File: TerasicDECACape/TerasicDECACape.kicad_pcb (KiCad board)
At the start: 4 copper layers, 61.3 x 66.3 mm, 34 parts, among them CN1 NASB0-S6701-TS50, CN2 NASB0-S6701-TS50, J1 MiSTer SDRAM Module, J2 USB_A, J3 Conn_01x03_Male, J4 Conn_02x06_Odd_Even, M1 Sipeed Lichee, P8 BeagleBone_Black_Header, P9 BeagleBone_Black_Header, SW1 TS-1187A-B-A-B, SW2 TS-1187A-B-A-B

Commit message: tidy, make it ready for production
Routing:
- net +3V3: track 8.53 -> 15.4 mm, vias 0 -> 6
- net /PB8_UART0_TX: vias 1 -> 2
- net /PB9_UART0_RX: vias 1 -> 2
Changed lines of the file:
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@@
     (fp_line (start 2.12 1.09) (end 0.93 1.09) (layer "F.SilkS") (width 0.15))
     (fp_line (start -2.27 -0.94) (end -2.27 0.94) (layer "F.SilkS") (width 0.15))
-    (fp_arc (start 0.001269 0.002199) (mid -0.112199 -0.41873) (end 0 -0.84) (layer "F.SilkS") (width 0.08))
+    (fp_arc (start 0.001269 0.002199) (mid -0.112199 -0.418731) (end 0 -0.84) (layer "F.SilkS") (width 0.08))
     (fp_arc (start -0.001269 -0.002199) (mid 0.112199 0.41873) (end 0 0.84) (layer "F.SilkS") (width 0.08))
     (fp_circle (center -1.6 0.8) (end -1.57 0.8) (layer "F.Fab") (width 0.06) (fill none))
@@
   (segment (start 115.1915 58.546) (end 115.1915 63.7438) (width 0.25) (layer "F.Cu") (net 65))
   (segment (start 116.3701 57.3674) (end 115.1915 58.546) (width 0.25) (layer "F.Cu") (net 65))
+  (via (at 128.5621 70.1294) (size 0.75) (drill 0.6) (layers "F.Cu" "B.Cu") (free) (net 65))
+  (via (at 137.9601 114.5794) (size 0.75) (drill 0.6) (layers "F.Cu" "B.Cu") (free) (net 65))
+  (via (at 137.9601 78.1304) (size 0.75) (drill 0.6) (layers "F.Cu" "B.Cu") (free) (net 65))
+  (via (at 128.5621 72.4154) (size 0.75) (drill 0.6) (layers "F.Cu" "B.Cu") (free) (net 65))
+  (via (at 140.2461 78.1304) (size 0.75) (drill 0.6) (layers "F.Cu" "B.Cu") (free) (net 65))
+  (via (at 140.2461 114.5794) (size 0.75) (drill 0.6) (layers "F.Cu" "B.Cu") (free) (net 65))
+  (segment (start 137.9601 114.5794) (end 140.2461 114.5794) (width 0.6) (layer "B.Cu") (net 65))
+  (segment (start 137.9601 78.1304) (end 140.2461 78.1304) (width 0.6) (layer "B.Cu") (net 65))
+  (segment (start 128.5621 72.4154) (end 128.5621 70.1294) (width 0.6) (layer "B.Cu") (net 65))
   (segment (start 134.4001 117.3324) (end 137.0701 117.3324) (width 0.3) (layer "F.Cu") (net 66))
   (segment (start 124.5201 68.7324) (end 125.0701 68.1824) (width 1.5) (layer "F.Cu") (net 66))
@@
   (segment (start 136.11571 99.8324) (end 150.267905 113.984595) (width 0.3) (layer "F.Cu") (net 155))
   (via (at 150.267905 113.984595) (size 0.6) (drill 0.4) (layers "F.Cu" "B.Cu") (net 155))
-  (segment (start 165.9915 119.441) (end 167.1701 118.2624) (width 0.25) (layer "B.Cu") (net 155))
-  (segment (start 153.20931 116.926) (end 155.72431 119.441) (width 0.25) (layer "B.Cu") (net 155))
-  (segment (start 155.72431 119.441) (end 165.9915 119.441) (width 0.25) (layer "B.Cu") (net 155))
-  (segment (start 150.267905 113.984595) (end 153.20931 116.926) (width 0.3) (layer "B.Cu") (net 155))
+  (segment (start 150.267905 113.984595) (end 150.884611 113.367889) (width 0.25) (layer "B.Cu") (net 155))
+  (segment (start 157.2641 115.4684) (end 162.5981 115.4684) (width 0.25) (layer "B.Cu") (net 155))
+  (segment (start 164.227589 117.097889) (end 166.005589 117.097889) (width 0.25) (layer "B.Cu") (net 155))
+  (segment (start 166.005589 117.097889) (end 167.1701 118.2624) (width 0.25) (layer "B.Cu") (net 155))
+  (segment (start 162.5981 115.4684) (end 164.227589 117.097889) (width 0.25) (layer "B.Cu") (net 155))
+  (segment (start 155.163589 113.367889) (end 157.2641 115.4684) (width 0.25) (layer "B.Cu") (net 155))
+  (segment (start 150.884611 113.367889) (end 155.163589 113.367889) (width 0.25) (layer "B.Cu") (net 155))
   (segment (start 136.5201 99.3324) (end 151.1701 113.9824) (width 0.3) (layer "F.Cu") (net 156))
   (segment (start 134.3901 99.3324) (end 136.5201 99.3324) (width 0.3) (layer "F.Cu") (net 156))
   (via (at 151.1701 113.9824) (size 0.6) (drill 0.4) (layers "F.Cu" "B.Cu") (net 156))
-  (segment (start 152.9101 115.7224) (end 155.4501 118.2624) (width 0.25) (layer "B.Cu") (net 156))
-  (segment (start 155.4501 118.2624) (end 164.6301 118.2624) (width 0.25) (layer "B.Cu") (net 156))
-  (segment (start 151.1701 113.9824) (end 152.9101 115.7224) (width 0.3) (layer "B.Cu") (net 156))
+  (segment (start 154.8891 113.9824) (end 157.2641 116.3574) (width 0.25) (layer "B.Cu") (net 156))
+  (segment (start 157.2641 116.3574) (end 162.7251 116.3574) (width 0.25) (layer "B.Cu") (net 156))
+  (segment (start 162.7251 116.3574) (end 164.6301 118.2624) (width 0.25) (layer "B.Cu") (net 156))
+  (segment (start 151.1701 113.9824) (end 154.8891 113.9824) (width 0.25) (layer "B.Cu") (net 156))
   (segment (start 125.7451 91.9324) (end 123.5451 94.1324) (width 0.3) (layer "F.Cu") (net 157))
   (segment (start 123.5451 94.1324) (end 117.6401 94.1324) (width 0.3) (layer "F.Cu") (net 157))
@@
   (segment (start 130.4701 76.6824) (end 130.4701 76.6719) (width 0.3) (layer "F.Cu") (net 166))
   (segment (start 130.4701 76.6719) (end 130.9701 76.1719) (width 0.3) (layer "F.Cu") (net 166))
+  (segment (start 134.6581 72.2884) (end 134.7001 72.2464) (width 0.25) (layer "F.Cu") (net 166))
   (segment (start 126.8501 93.4324) (end 128.148064 93.4324) (width 0.3) (layer "F.Cu") (net 166))
   (segment (start 135.2201 63.7824) (end 135.2201 65.3124) (width 0.3) (layer "F.Cu") (net 166))
+  (segment (start 134.7001 72.2464) (end 134.7001 65.8324) (width 0.25) (layer "F.Cu") (net 166))
   (segment (start 130.4701 91.110364) (end 130.4701 76.6824) (width 0.3) (layer "F.Cu") (net 166))
   (segment (start 128.148064 93.4324) (end 130.4701 91.110364) (width 0.3) (layer "F.Cu") (net 166))
+  (via (at 134.6581 72.2884) (size 0.6) (drill 0.4) (layers "F.Cu" "B.Cu") (net 166))
   (via (at 130.9701 76.1719) (size 0.6) (drill 0.4) (layers "F.Cu" "B.Cu") (net 166))
+  (segment (start 134.6701 74.163844) (end 134.6701 72.3004) (width 0.25) (layer "B.Cu") (net 166))
   (segment (start 132.662044 76.1719) (end 134.6701 74.163844) (width 0.3) (layer "B.Cu") (net 166))
+  (segment (start 134.6701 72.3004) (end 134.6581 72.2884) (width 0.25) (layer "B.Cu") (net 166))
   (segment (start 130.9701 76.1719) (end 132.662044 76.1719) (width 0.3) (layer "B.Cu") (net 166))
-  (segment (start 134.7001 70.1024) (end 134.7001 65.8324) (width 0.3) (layer "B.Cu") (net 166))
-  (segment (start 134.6701 70.1324) (end 134.7001 70.1024) (width 0.3) (layer "B.Cu") (net 166))
-  (segment (start 134.6701 74.163844) (end 134.6701 70.1324) (width 0.3) (layer "B.Cu") (net 166))
   (segment (start 127.9551 92.9324) (end 129.6701 91.2174) (width 0.3) (layer "F.Cu") (net 167))
   (segment (start 126.8501 92.9324) (end 127.9551 92.9324) (width 0.3) (layer "F.Cu") (net 167))
+  (segment (start 133.3881 72.2884) (end 132.1601 71.0604) (width 0.25) (layer "F.Cu") (net 167))
   (segment (start 129.6701 91.2174) (end 129.6701 76.4324) (width 0.3) (layer "F.Cu") (net 167))
   (segment (start 129.6701 76.4324) (end 129.6701 76.1824) (width 0.3) (layer "F.Cu") (net 167))
+  (segment (start 132.1601 71.0604) (end 132.1601 65.8324) (width 0.25) (layer "F.Cu") (net 167))
   (segment (start 129.6701 76.1824) (end 130.3201 75.5324) (width 0.3) (layer "F.Cu") (net 167))
   (segment (start 131.6701 65.3424) (end 132.1601 65.8324) (width 0.3) (layer "F.Cu") (net 167))
   (segment (start 131.6701 63.8324) (end 131.6701 65.3424) (width 0.3) (layer "F.Cu") (net 167))
+  (via (at 133.3881 72.2884) (size 0.6) (drill 0.4) (layers "F.Cu" "B.Cu") (net 167))
   (via (at 130.3201 75.5324) (size 0.6) (drill 0.4) (layers "F.Cu" "B.Cu") (net 167))
   (segment (start 130.3201 75.5324) (end 132.60858 75.5324) (width 0.3) (layer "B.Cu") (net 167))
-  (segment (start 133.4601 74.68088) (end 133.4601 67.1324) (width 0.3) (layer "B.Cu") (net 167))
-  (segment (start 133.4601 67.1324) (end 132.1601 65.8324) (width 0.3) (layer "B.Cu") (net 167))
+  (segment (start 133.4601 74.68088) (end 133.4601 72.3604) (width 0.25) (layer "B.Cu") (net 167))
+  (segment (start 133.4601 72.3604) (end 133.3881 72.2884) (width 0.25) (layer "B.Cu") (net 167))
   (segment (start 132.60858 75.5324) (end 133.4601 74.68088) (width 0.3) (layer "B.Cu") (net 167))
   (segment (start 155.5651 116.0624) (end 155.5651 115.2174) (width 0.3) (layer "F.Cu") (net 168))

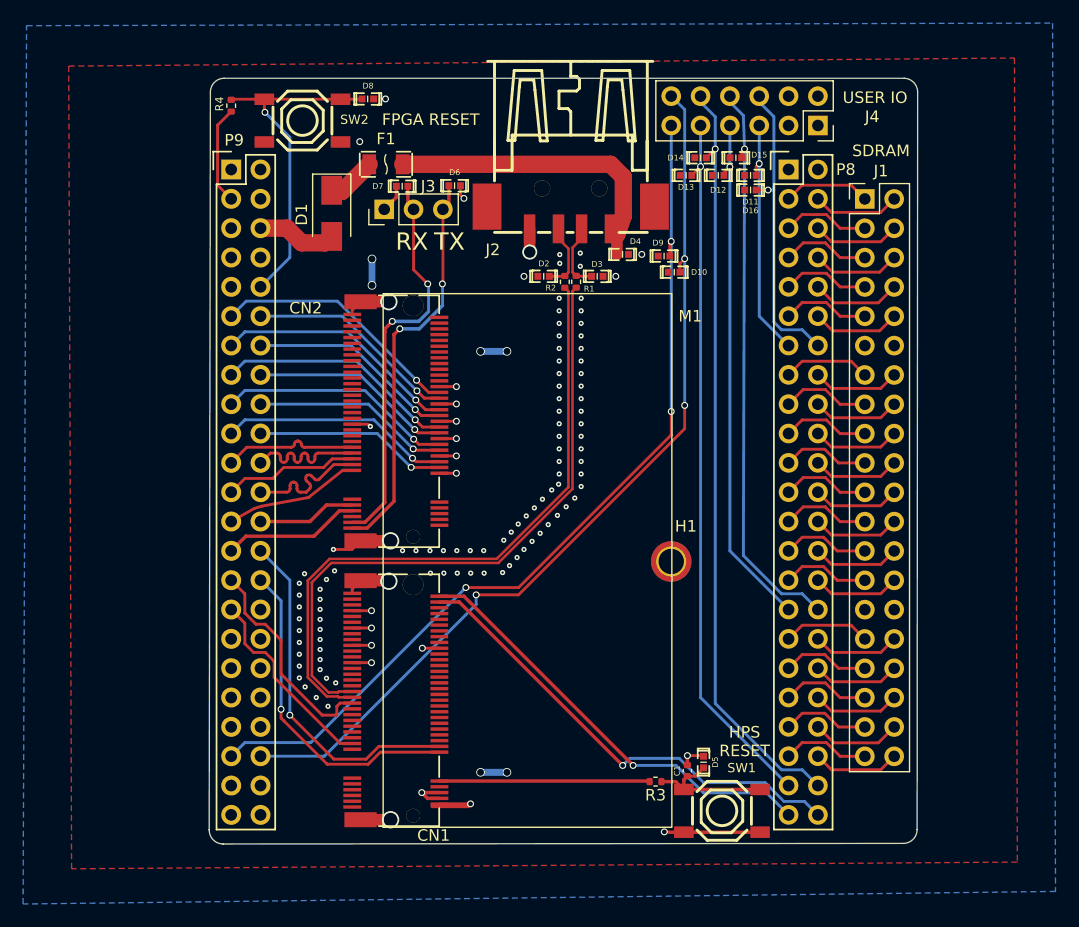
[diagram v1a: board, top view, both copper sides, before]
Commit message: fix swapped SDRAM net names on both headers, fix impedance on USB diff pair, add SPI termination resistors
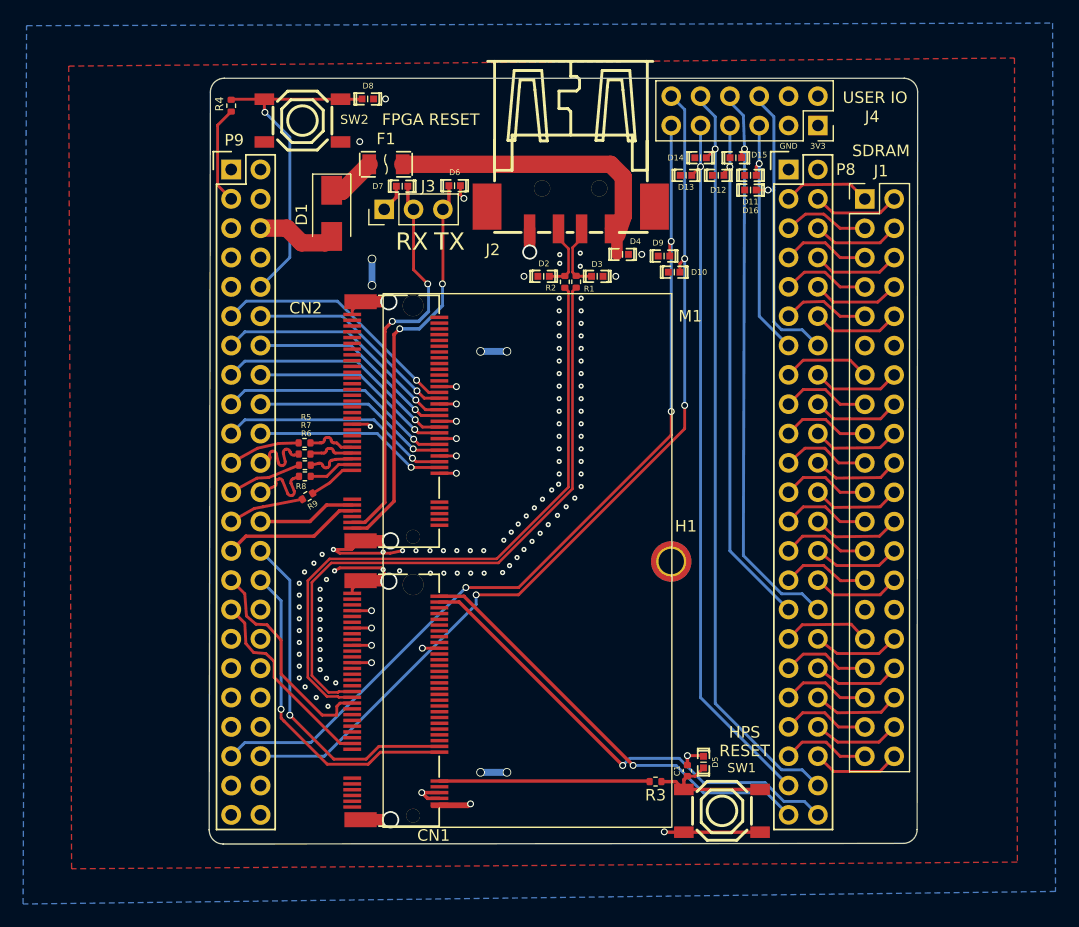
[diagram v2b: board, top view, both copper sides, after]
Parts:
- added R5: 47R, Resistor_SMD:R_0402_1005Metric, F.Cu at (122.7, 86.1)
- added R6: 47R, Resistor_SMD:R_0402_1005Metric, F.Cu at (122.7, 88.0)
- added R7: 47R, Resistor_SMD:R_0402_1005Metric, F.Cu at (122.7, 87.0)
- added R8: 47R, Resistor_SMD:R_0402_1005Metric, F.Cu at (122.7, 89.0)
- added R9: 47R, Resistor_SMD:R_0402_1005Metric, F.Cu at (123.0, 90.7)
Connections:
- J1 pad 13: /RAM_DQ12 -> /RAM_DQ13
- J1 pad 14: /RAM_DQ13 -> /RAM_DQ12
- J1 pad 15: /RAM_DQ10 -> /RAM_DQ11
- J1 pad 16: /RAM_DQ11 -> /RAM_DQ10
- J1 pad 17: /RAM_DQ8 -> /RAM_DQ9
- J1 pad 18: /RAM_DQ9 -> /RAM_DQ8
- J1 pad 19: /RAM_CLK -> /RAM_A12
- J1 pad 20: /RAM_A12 -> /RAM_CLK
- J1 pad 21: /RAM_A11 -> /RAM_A9
- J1 pad 22: /RAM_A9 -> /RAM_A11
- J1 pad 23: /RAM_A8 -> /RAM_A7
- J1 pad 24: /RAM_A7 -> /RAM_A8
- J1 pad 25: /RAM_A6 -> /RAM_A5
- J1 pad 26: /RAM_A5 -> /RAM_A6
- J1 pad 27: /RAM_A4 -> /RAM_WE
- J1 pad 28: /RAM_WE -> /RAM_A4
- P8 pad 15: /RAM_DQ12 -> /RAM_DQ13
- P8 pad 16: /RAM_DQ13 -> /RAM_DQ12
- P8 pad 17: /RAM_DQ10 -> /RAM_DQ11
- P8 pad 18: /RAM_DQ11 -> /RAM_DQ10
- P8 pad 19: /RAM_DQ8 -> /RAM_DQ9
- P8 pad 20: /RAM_DQ9 -> /RAM_DQ8
- P8 pad 21: /RAM_CLK -> /RAM_A12
- P8 pad 22: /RAM_A12 -> /RAM_CLK
- P8 pad 23: /RAM_A11 -> /RAM_A9
- P8 pad 24: /RAM_A9 -> /RAM_A11
- P8 pad 25: /RAM_A8 -> /RAM_A7
- P8 pad 26: /RAM_A7 -> /RAM_A8
- P8 pad 27: /RAM_A6 -> /RAM_A5
- P8 pad 28: /RAM_A5 -> /RAM_A6
- P8 pad 29: /RAM_A4 -> /RAM_WE
- P8 pad 30: /RAM_WE -> /RAM_A4
- P9 pad 21: /PD10 -> Net-(P9-Pad21)
- P9 pad 22: /PD11 -> Net-(P9-Pad22)
- P9 pad 23: /PD12 -> Net-(P9-Pad23)
- P9 pad 24: /PD13 -> Net-(P9-Pad24)
- P9 pad 25: /PD14 -> Net-(P9-Pad25)
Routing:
- net GND: track 53.7 -> 65.3 mm, vias 118 -> 123
- net /PD14: track 11.7 -> 4.01 mm
- net /PD13: track 11.5 -> 4.01 mm
- net Net-(P9-Pad24): track 0.00 -> 7.48 mm
- net /PD12: track 11.7 -> 4.22 mm
- net /PD11: track 11.5 -> 4.08 mm
- net /PD10: track 11.6 -> 4.27 mm
- net Net-(P9-Pad25): track 0.00 -> 6.54 mm
- net Net-(P9-Pad22): track 0.00 -> 6.40 mm
- net Net-(P9-Pad23): track 0.00 -> 6.39 mm
- net Net-(P9-Pad21): track 0.00 -> 6.22 mm
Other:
- board text added: "3V3"
- board text added: "GND"
